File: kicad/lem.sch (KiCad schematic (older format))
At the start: 24 parts

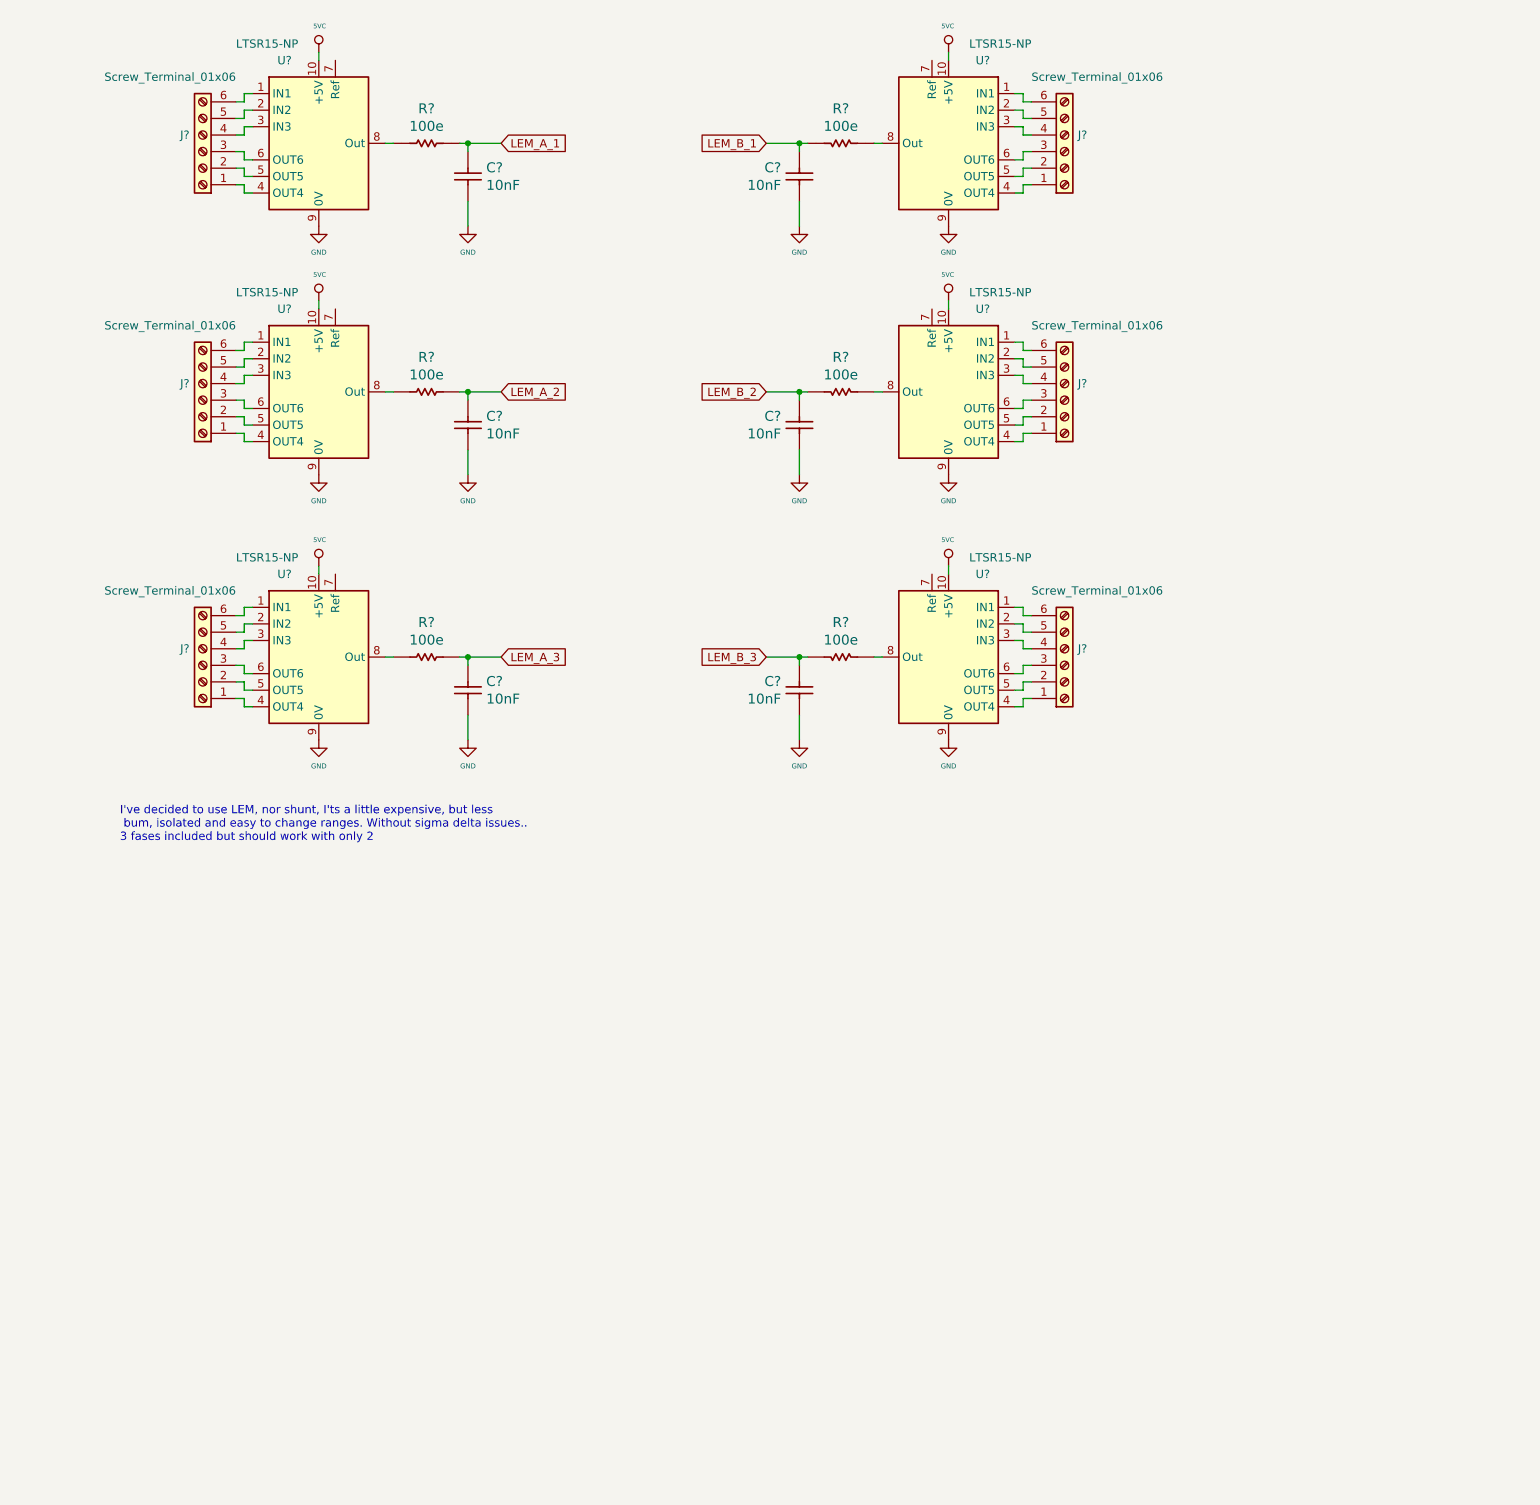
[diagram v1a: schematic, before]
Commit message: added shunt using sigma delta, just fot 1 channel
I've added a sigma delta isolated sampler for use with shunt in phase
measurement. 'cose it seems is the best accuracy method for current
measurement, but it implies a lot of componentes, 8 PWM lines to
generate the sigma delta clk, or maybe I'd use only one clk for all
sigma deltas, ..I've to think about it, but it seems that should be
better than Hall.. working on that
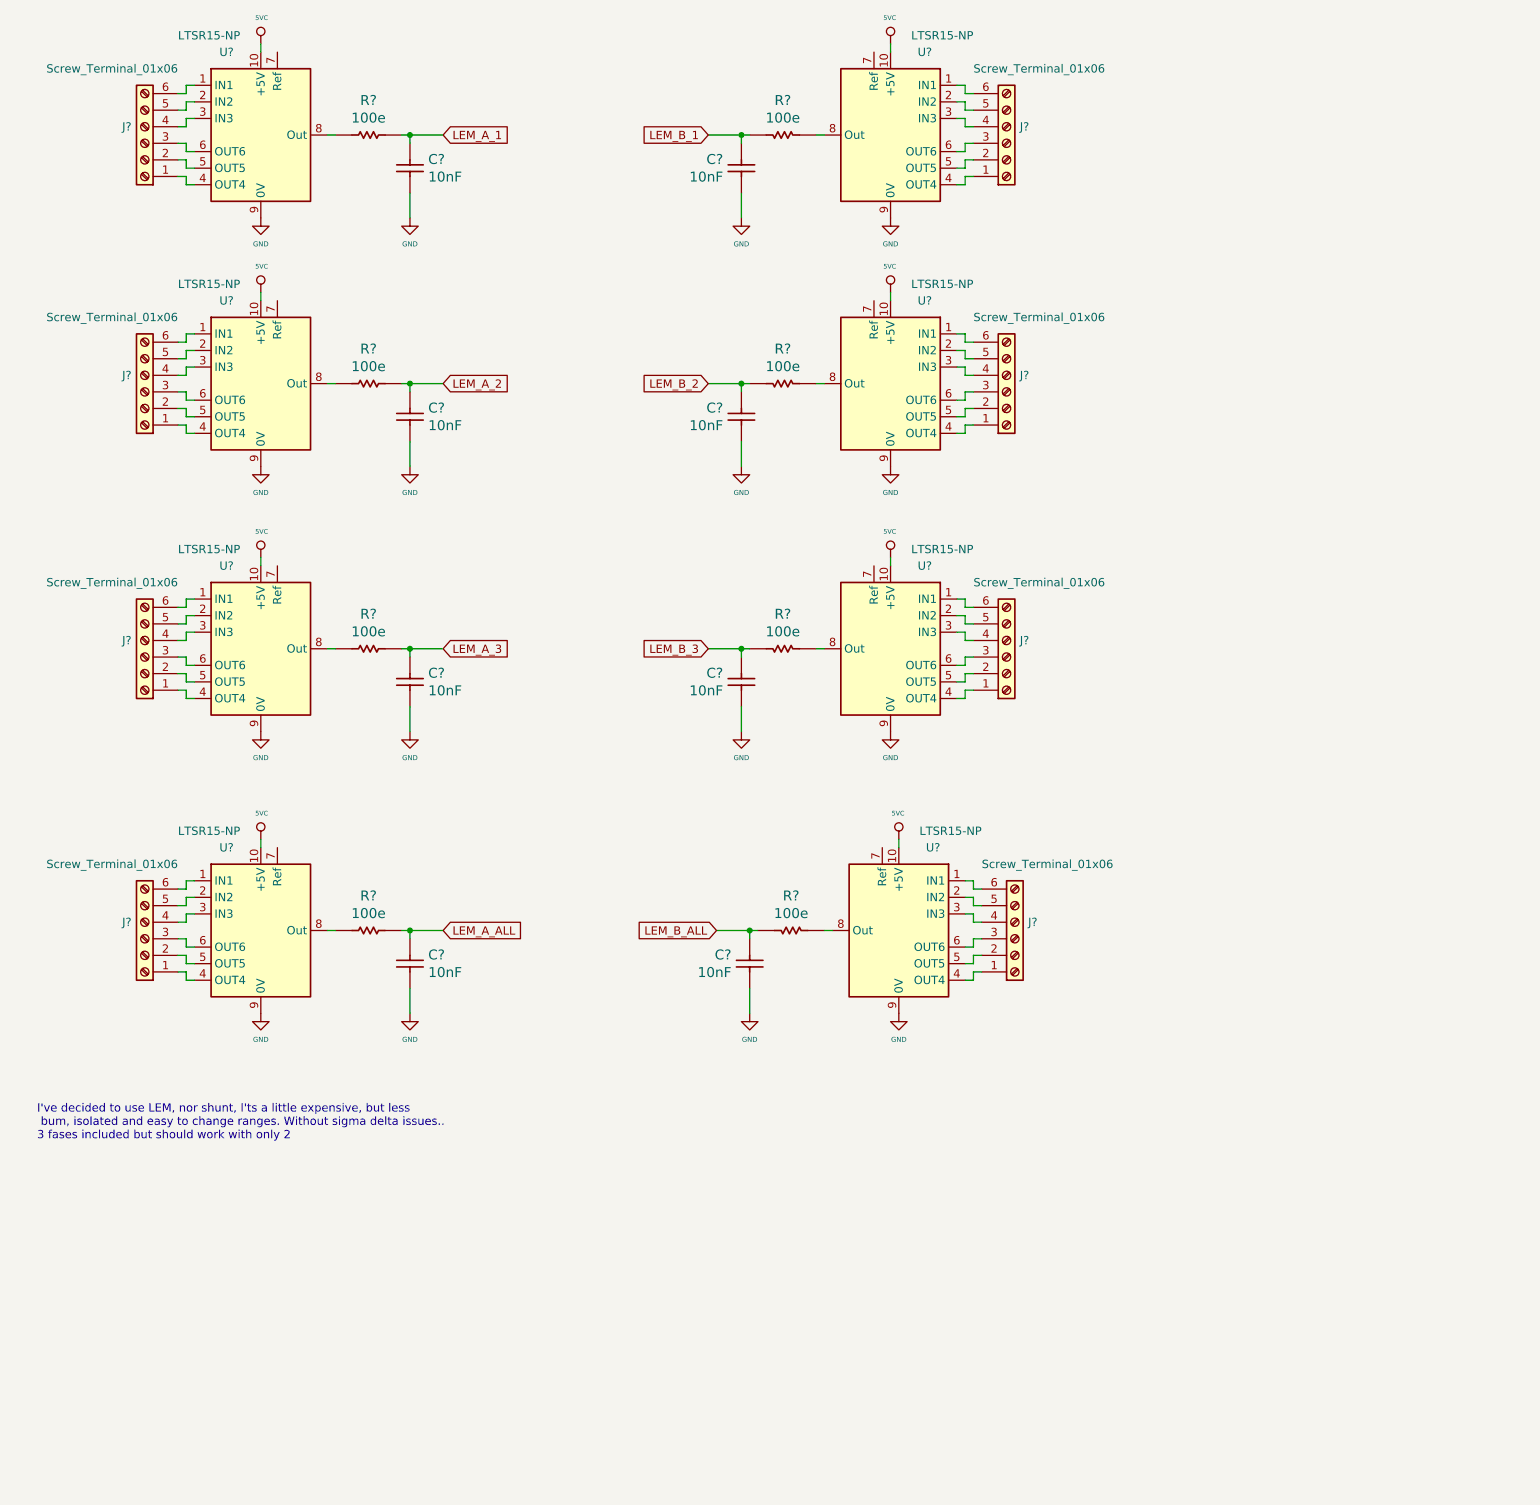
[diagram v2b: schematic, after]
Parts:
- added C? (x2): 10nF, symbol servo:Capacitor
- added J? (x2): Screw_Terminal_01x06, symbol Connector:Screw_Terminal_01x06
- added R? (x2): 100e, symbol servo:Resistor
- added U? (x2): LTSR15-NP, Sensor_Current:LEM_LTSR-NP, symbol servo:LTSR15-NP
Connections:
- net 5VC: now also U?.10 (+5V), U?.10 (+5V)
- net GND: now also C?.1, C?.1, U?.9 (0V), U?.9 (0V)
- new net: J?.6 (Pin_6), U?.1 (IN1) (x2)
- new net: J?.5 (Pin_5), U?.2 (IN2) (x2)
- new net: J?.4 (Pin_4), U?.3 (IN3) (x2)
- new net: J?.1 (Pin_1), U?.4 (OUT4) (x2)
- new net: J?.2 (Pin_2), U?.5 (OUT5) (x2)
- new net: J?.3 (Pin_3), U?.6 (OUT6) (x2)
- new net: R?.1, U?.8 (Out) (x2)
- new net LEM_A_ALL: C?.2, R?.2
- new net LEM_B_ALL: C?.2, R?.2
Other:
- moved on the sheet: C?, J?, R?, U?

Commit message: Come back to moldova to finish schematics and begin layout
I've started again from Moldova to discuss with Alexander the details.
I'm now working with schematics requeriments.
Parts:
- removed C? (x4): 10nF, symbol servo:Capacitor
- removed J? (x4): Screw_Terminal_01x06, symbol Connector:Screw_Terminal_01x06
- removed R? (x4): 100e, symbol servo:Resistor
- removed U? (x4): LTSR15-NP, Sensor_Current:LEM_LTSR-NP, symbol servo:LTSR15-NP
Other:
- note added: "I've decided to add some LEM, I'ts a little expensive, but less\n bom, isolated and easy to change ranges. Without sigma delta issues..\nshould work with only 2 phases\n"
- note removed: "I've decided to use LEM, nor shunt, I'ts a little expensive, but less\n bum, isolated and easy to change ranges. Without sigma delta issues..\n3 fases included but should work with only 2\n\n"
